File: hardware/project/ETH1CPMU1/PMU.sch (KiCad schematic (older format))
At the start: 58 parts, among them K1401 HE3621A0510, K1402 HE3621A0510, K1403 HE3621A0510, K1404 HE3621A0510, K1405 HE3621A0510, K1406 HE3621A0510, K1407 HE3621A0510, K1408 HE3621A0510, Q1401 BC847, Q1402 BC847, Q1403 BC847, Q1404 BC847, Q1405 BC847, Q1406 BC847, Q1407 BC847, Q1408 BC847, U1401 AD5520, U1402 AD8010, U1403 DG419LEUA

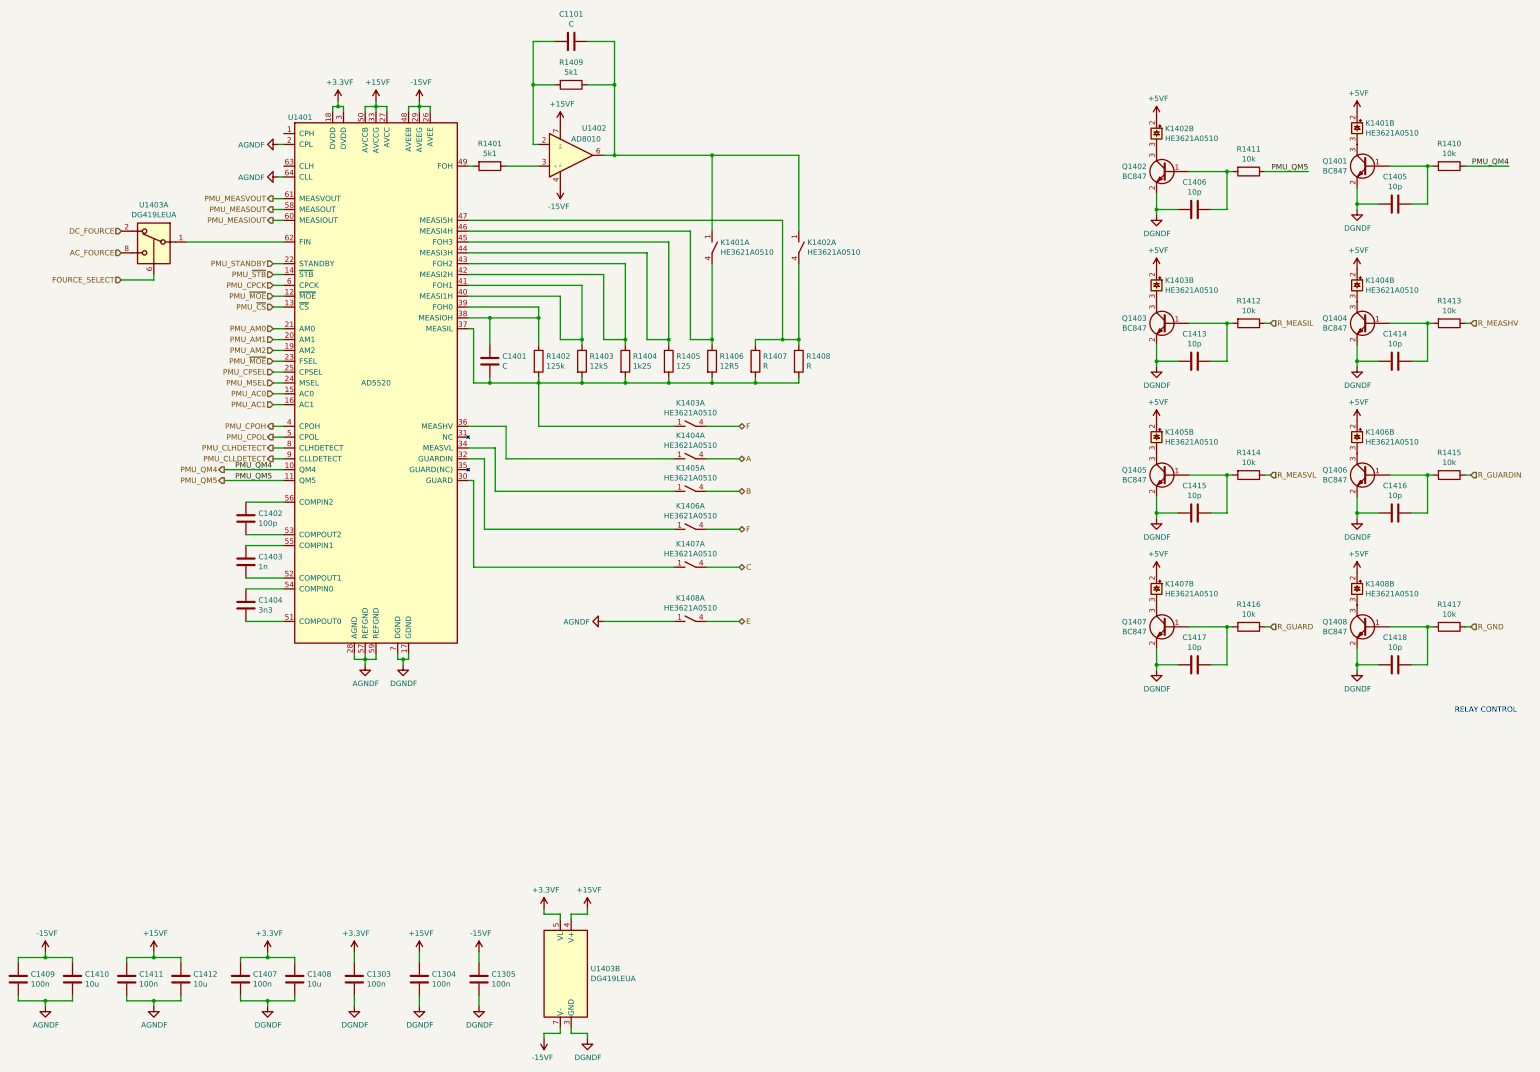
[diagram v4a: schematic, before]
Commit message: New footprint development, changes in schematics.
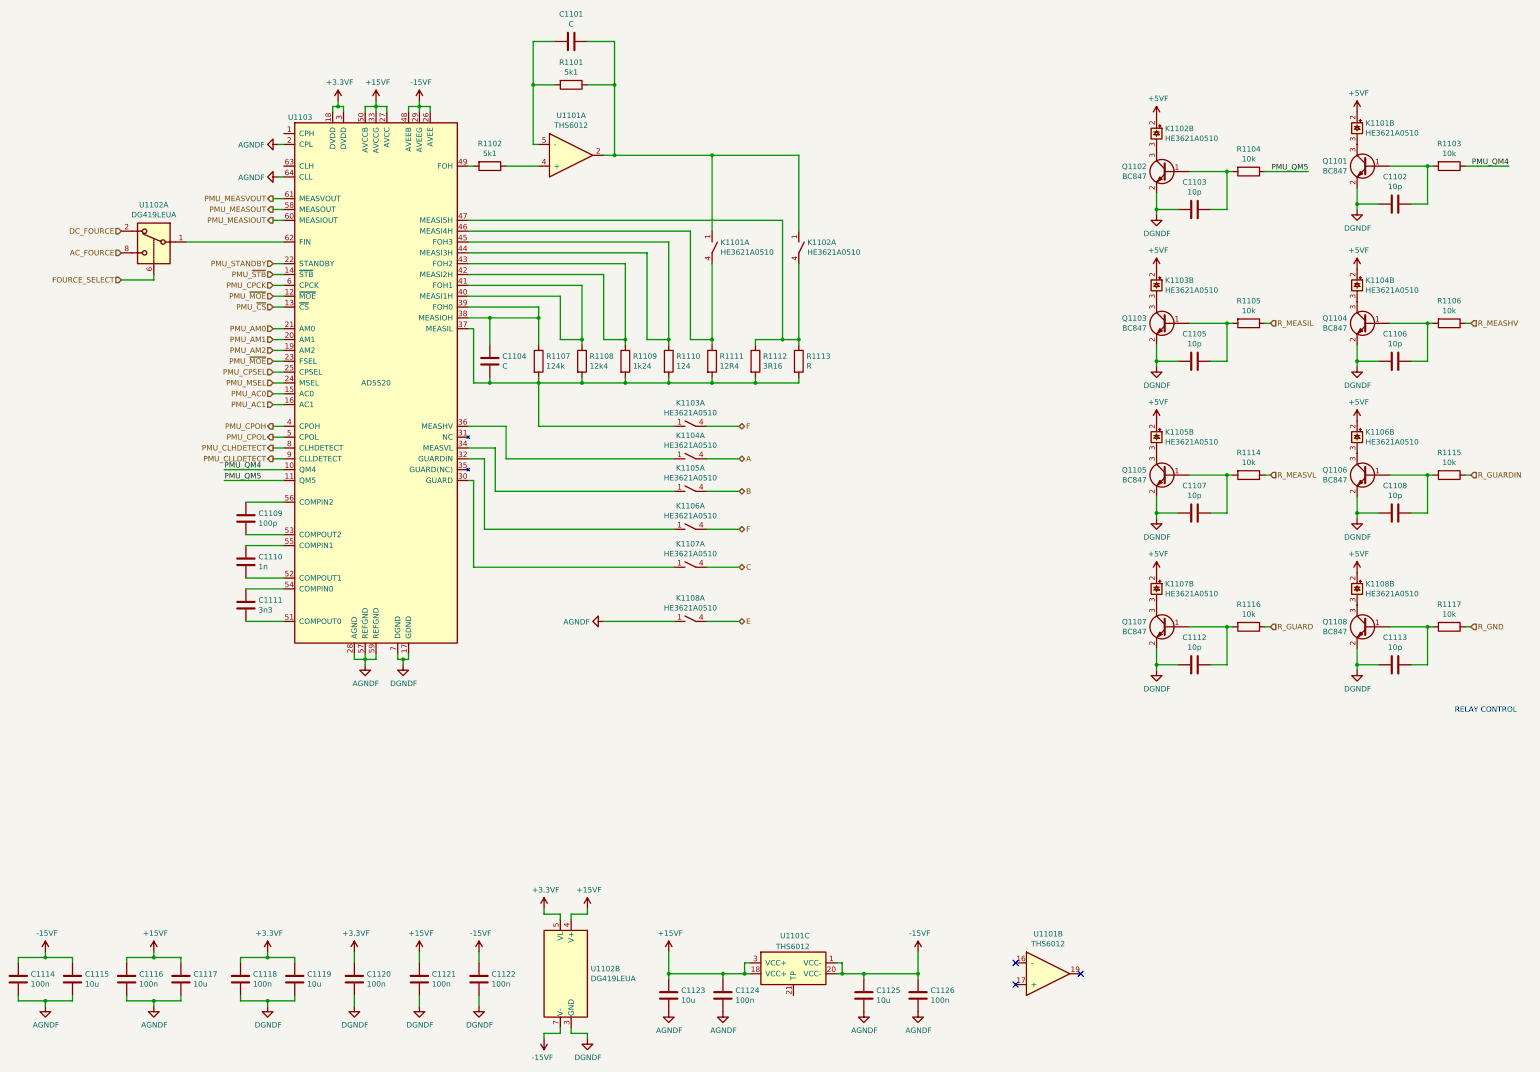
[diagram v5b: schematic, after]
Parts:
- removed U1402: AD8010, symbol ETH1CPMU1:AD8010
- added C1123, C1125: 10u, Capacitor_SMD:C_1206_3216Metric_Pad1.42x1.75mm_HandSolder, symbol Device:C
- added C1124, C1126: 100n, Capacitor_SMD:C_0603_1608Metric_Pad1.05x0.95mm_HandSolder, symbol Device:C
- added U1101: THS6012, symbol ETH1CPMU1:THS6012
- K1101: renamed from K1401; footprint (none) -> ETH1CPMU1:HE360_x-5050462-8
- K1102: renamed from K1402; footprint (none) -> ETH1CPMU1:HE360_x-5050462-8
- K1103: renamed from K1403; footprint (none) -> ETH1CPMU1:HE360_x-5050462-8
- K1104: renamed from K1404; footprint (none) -> ETH1CPMU1:HE360_x-5050462-8
- K1105: renamed from K1405; footprint (none) -> ETH1CPMU1:HE360_x-5050462-8
- K1106: renamed from K1406; footprint (none) -> ETH1CPMU1:HE360_x-5050462-8
- K1107: renamed from K1407; footprint (none) -> ETH1CPMU1:HE360_x-5050462-8
- K1108: renamed from K1408; footprint (none) -> ETH1CPMU1:HE360_x-5050462-8
- R1107: renamed from R1402; value 125k -> 124k
- R1108: renamed from R1403; value 12k5 -> 12k4
- R1109: renamed from R1404; value 1k25 -> 1k24
- R1110: renamed from R1405; value 125 -> 124
- R1111: renamed from R1406; value 12R5 -> 12R4
- R1112: renamed from R1407; value R -> 3R16; footprint (none) -> Resistor_SMD:R_0603_1608Metric_Pad1.05x0.95mm_HandSolder
- R1113: renamed from R1408; footprint (none) -> Resistor_SMD:R_0603_1608Metric_Pad1.05x0.95mm_HandSolder
- U1103: renamed from U1401; footprint (none) -> Package_QFP:LQFP-64_10x10mm_P0.5mm
- renumbered C1405 to C1102, C1406 to C1103, C1401 to C1104, C1413 to C1105, C1414 to C1106, C1415 to C1107, C1416 to C1108, C1402 to C1109, C1403 to C1110, C1404 to C1111, C1417 to C1112, C1418 to C1113, C1409 to C1114, C1410 to C1115, C1411 to C1116, C1412 to C1117, C1407 to C1118, C1408 to C1119, C1303 to C1120, C1304 to C1121, C1305 to C1122, Q1401 to Q1101, Q1402 to Q1102, Q1403 to Q1103, Q1404 to Q1104, Q1405 to Q1105, Q1406 to Q1106, Q1407 to Q1107, Q1408 to Q1108, R1409 to R1101, R1401 to R1102, R1410 to R1103, R1411 to R1104, R1412 to R1105, R1413 to R1106, R1414 to R1114, R1415 to R1115, R1416 to R1116, R1417 to R1117, U1403 to U1102
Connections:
- net +15VF: now also C1123.1, C1124.1, U1101.18 (VCC+), U1101.3 (VCC+)
- net -15VF: now also C1125.1, C1126.1, U1101.1 (VCC-), U1101.20 (VCC-)
- net AGNDF: now also C1123.2, C1124.2, C1125.2, C1126.2
- net at C1101.2, R1101.2: now also U1101.5 (-)
- net at R1102.1: now also U1101.4 (+)
- net at C1101.1, K1101.1, K1102.1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: now also U1101.2
- no-connect marks 0 -> 3

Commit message: Schematic and PCB design.
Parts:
- U1101: footprint (none) -> ETH1CPMU1:PowerPAD
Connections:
- net AGNDF: now also U1101.21 (TP)
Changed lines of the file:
@@
 	5950 9550 5950 9600
 $Comp
-L ETH1CPMU1:DGNDF #PWR01146
+L ETH1CPMU1:DGNDF #PWR01147
 U 1 1 5E2E5E34
 P 6100 10700
-F 0 "#PWR01146" H 6100 10450 50  0001 C CNN
+F 0 "#PWR01147" H 6100 10450 50  0001 C CNN
 F 1 "DGNDF" H 6105 10527 50  0000 C CNN
 F 2 "" H 6100 10700 50  0001 C CNN
@@
 	5950 10650 5950 10600
 $Comp
-L ETH1CPMU1:-15VF #PWR01145
+L ETH1CPMU1:-15VF #PWR01146
 U 1 1 5E2F7E49
 P 5700 10700
-F 0 "#PWR01145" H 5700 10550 50  0001 C CNN
+F 0 "#PWR01146" H 5700 10550 50  0001 C CNN
 F 1 "-15VF" H 5715 10873 50  0000 C CNN
 F 2 "" H 5700 10700 50  0001 C CNN
@@
 Connection ~ 6350 1900
 $Comp
-L ETH1CPMU1:THS6012 U1101
+L ETH1CPMU1:THS6012 U?
 U 1 1 5DFE61F7
 P 5900 2550
+AR Path="/5DFE61F7" Ref="U?"  Part="1"
+AR Path="/5DF36410/5DFE61F7" Ref="U1101"  Part="1"
 F 0 "U1101" H 5950 2917 50  0000 C CNN
 F 1 "THS6012" H 5950 2826 50  0000 C CNN
-F 2 "" H 5900 2900 50  0001 C CNN
+F 2 "ETH1CPMU1:PowerPAD" H 5900 2900 50  0001 C CNN
 F 3 "" H 5900 2900 50  0001 C CNN
 	1    5900 2550
@@
 $EndComp
 $Comp
-L ETH1CPMU1:THS6012 U1101
+L ETH1CPMU1:THS6012 U?
 U 2 1 5DFE6F36
 P 10300 10100
+AR Path="/5DFE6F36" Ref="U?"  Part="2"
+AR Path="/5DF36410/5DFE6F36" Ref="U1101"  Part="2"
 F 0 "U1101" H 10350 10467 50  0000 C CNN
 F 1 "THS6012" H 10350 10376 50  0000 C CNN
-F 2 "" H 10300 10450 50  0001 C CNN
+F 2 "ETH1CPMU1:PowerPAD" H 10300 10450 50  0001 C CNN
 F 3 "" H 10300 10450 50  0001 C CNN
 	2    10300 10100
@@
 $EndComp
 $Comp
-L ETH1CPMU1:THS6012 U1101
+L ETH1CPMU1:THS6012 U?
 U 3 1 5DFE7B2F
 P 8000 10050
+AR Path="/5DFE7B2F" Ref="U?"  Part="3"
+AR Path="/5DF36410/5DFE7B2F" Ref="U1101"  Part="3"
 F 0 "U1101" V 7700 9900 50  0000 L CNN
 F 1 "THS6012" V 7800 9900 50  0000 L CNN
-F 2 "" H 8000 10400 50  0001 C CNN
+F 2 "ETH1CPMU1:PowerPAD" H 8000 10400 50  0001 C CNN
 F 3 "" H 8000 10400 50  0001 C CNN
 	3    8000 10050
@@
 $EndComp
 $Comp
-L ETH1CPMU1:AGNDF #PWR01143
+L ETH1CPMU1:AGNDF #PWR01144
 U 1 1 5E286227
 P 8650 10450
-F 0 "#PWR01143" H 8650 10200 50  0001 C CNN
+F 0 "#PWR01144" H 8650 10200 50  0001 C CNN
 F 1 "AGNDF" H 8655 10277 50  0000 C CNN
 F 2 "" H 8650 10450 50  0001 C CNN
@@
 $EndComp
 $Comp
-L ETH1CPMU1:AGNDF #PWR01144
+L ETH1CPMU1:AGNDF #PWR01145
 U 1 1 5E28699B
 P 9150 10450
-F 0 "#PWR01144" H 9150 10200 50  0001 C CNN
+F 0 "#PWR01145" H 9150 10200 50  0001 C CNN
 F 1 "AGNDF" H 9155 10277 50  0000 C CNN
 F 2 "" H 9150 10450 50  0001 C CNN
@@
 NoConn ~ 10050 10200
 NoConn ~ 10650 10100
+$Comp
+L ETH1CPMU1:AGNDF #PWR01143
+U 1 1 5E1FF395
+P 8000 10450
+F 0 "#PWR01143" H 8000 10200 50  0001 C CNN
+F 1 "AGNDF" H 8005 10277 50  0000 C CNN
+F 2 "" H 8000 10450 50  0001 C CNN
+F 3 "" H 8000 10450 50  0001 C CNN
+	1    8000 10450
+	1    0    0    -1
+$EndComp
+Wire Wire Line
+	8000 10450 8000 10300
 $EndSCHEMATC

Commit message: Schematic design
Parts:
- renumbered C1101 to C1401, C1102 to C1402, C1103 to C1403, C1104 to C1404, C1105 to C1405, C1106 to C1406, C1107 to C1407, C1108 to C1408, C1109 to C1409, C1110 to C1410, C1111 to C1411, C1112 to C1412, C1113 to C1413, C1114 to C1414, C1115 to C1415, C1116 to C1416, C1117 to C1417, C1118 to C1418, C1119 to C1419, C1120 to C1420, C1121 to C1421, C1122 to C1422, C1123 to C1423, C1124 to C1424, C1125 to C1425, C1126 to C1426, K1101 to K1401, K1102 to K1402, K1103 to K1403, K1104 to K1404, K1105 to K1405, K1106 to K1406, K1107 to K1407, K1108 to K1408, Q1101 to Q1401, Q1102 to Q1402, Q1103 to Q1403, Q1104 to Q1404, Q1105 to Q1405, Q1106 to Q1406, Q1107 to Q1407, Q1108 to Q1408, R1101 to R1401, R1102 to R1402, R1103 to R1403, R1104 to R1404, R1105 to R1405, R1106 to R1406, R1107 to R1407, R1108 to R1408, R1109 to R1409, R1110 to R1410, R1111 to R1411, R1112 to R1412, R1113 to R1413, R1114 to R1414, R1115 to R1415, R1116 to R1416, R1117 to R1417, U1101 to U1401, U1102 to U1402, U1103 to U1403
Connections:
- net PMU_CPH: now reaches U1403.1 (CPH)
- net PMU_CLH: now reaches U1403.63 (CLH)

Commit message: PCB design.
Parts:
- C1415, C1417, C1419, C1423, C1425: footprint Capacitor_SMD:C_1206_3216Metric_Pad1.42x1.75mm_HandSolder -> Capacitor_SMD:C_0805_2012Metric_Pad1.15x1.40mm_HandSolder
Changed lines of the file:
@@
 F 0 "C1415" H 1465 10196 50  0000 L CNN
 F 1 "10u" H 1465 10105 50  0000 L CNN
-F 2 "Capacitor_SMD:C_1206_3216Metric_Pad1.42x1.75mm_HandSolder" H 1388 10000 50  0001 C CNN
+F 2 "Capacitor_SMD:C_0805_2012Metric_Pad1.15x1.40mm_HandSolder" H 1388 10000 50  0001 C CNN
 F 3 "~" H 1350 10150 50  0001 C CNN
 	1    1350 10150
@@
 F 0 "C1417" H 2465 10196 50  0000 L CNN
 F 1 "10u" H 2465 10105 50  0000 L CNN
-F 2 "Capacitor_SMD:C_1206_3216Metric_Pad1.42x1.75mm_HandSolder" H 2388 10000 50  0001 C CNN
+F 2 "Capacitor_SMD:C_0805_2012Metric_Pad1.15x1.40mm_HandSolder" H 2388 10000 50  0001 C CNN
 F 3 "~" H 2350 10150 50  0001 C CNN
 	1    2350 10150
@@
 F 0 "C1419" H 3515 10196 50  0000 L CNN
 F 1 "10u" H 3515 10105 50  0000 L CNN
-F 2 "Capacitor_SMD:C_1206_3216Metric_Pad1.42x1.75mm_HandSolder" H 3438 10000 50  0001 C CNN
+F 2 "Capacitor_SMD:C_0805_2012Metric_Pad1.15x1.40mm_HandSolder" H 3438 10000 50  0001 C CNN
 F 3 "~" H 3400 10150 50  0001 C CNN
 	1    3400 10150
@@
 F 0 "C1423" H 6965 10346 50  0000 L CNN
 F 1 "10u" H 6965 10255 50  0000 L CNN
-F 2 "Capacitor_SMD:C_1206_3216Metric_Pad1.42x1.75mm_HandSolder" H 6888 10150 50  0001 C CNN
+F 2 "Capacitor_SMD:C_0805_2012Metric_Pad1.15x1.40mm_HandSolder" H 6888 10150 50  0001 C CNN
 F 3 "~" H 6850 10300 50  0001 C CNN
 	1    6850 10300
@@
 F 0 "C1425" H 8765 10346 50  0000 L CNN
 F 1 "10u" H 8765 10255 50  0000 L CNN
-F 2 "Capacitor_SMD:C_1206_3216Metric_Pad1.42x1.75mm_HandSolder" H 8688 10150 50  0001 C CNN
+F 2 "Capacitor_SMD:C_0805_2012Metric_Pad1.15x1.40mm_HandSolder" H 8688 10150 50  0001 C CNN
 F 3 "~" H 8650 10300 50  0001 C CNN
 	1    8650 10300
